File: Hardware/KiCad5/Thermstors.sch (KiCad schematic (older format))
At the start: 27 parts, among them J4 Audio-Jack-2_Switch, J5 Audio-Jack-2_Switch, U3 4066, U4 LM358

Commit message: Update schematic
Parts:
- removed J4, J5: Audio-Jack-2_Switch, symbol CloudSmoker-rescue:Audio-Jack-2_Switch
- removed U4: LM358, symbol CloudSmoker-rescue:LM358
- added C?: 10nF, symbol device:C
- added C?: 0.1u, symbol device:C
- added J? (x2): AudioJack2_SwitchT, symbol Connector:AudioJack2_SwitchT
- added U? (x5): 4066, symbol 4xxx:4066
- added U? (x3): LM358, symbol Amplifier_Operational:LM358
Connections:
- net +3V3: now also C?.1, C?.1, U?.14 (VDD), U?.8 (V+)
- net CTL-A: now also U?.13
- net CTL-B: now also U?.5
- net GND: now also C?.2, C?.2, J?.S, J?.S, U?.4 (V-), U?.7 (VSS)
- net MUX: now also U?.2, U?.3
- net MeatADC: now also U?.1
- net PitADC: now also U?.4
- net at R?.1, R?.2: now also J?.T (x2)
- net at R23.1, R25.2: now also U?.1
- net at R18.1, R23.2: now also U?.2 (-)
- net at R16.1, R20.2: now also U?.3 (+)
- net at R17.1, R21.2: now also U?.5 (+)
- net at R19.1, R24.2: now also U?.6 (-)
- net at R24.1, R26.2: now also U?.7
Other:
- note added: "OpAmp Level Shifter \n(approx 0.2 - 1.15V output for ESP8266 ADC)"
- note added: "Place cap as close to \nPin14 Vdd as possible"
- note added: "add 10nF cap as close to \nsupply pin as possible"
- note removed: "Level Shifter \n(approx 0.2 - 1.15V output for ESP8266 ADC)"
- note removed: "add 10nF cap between opamp V+ and gnd. as as possible"
- moved on the sheet: C7, C8, C9, R13, R14, R15, R16, R17, R18, R19, R20, R21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

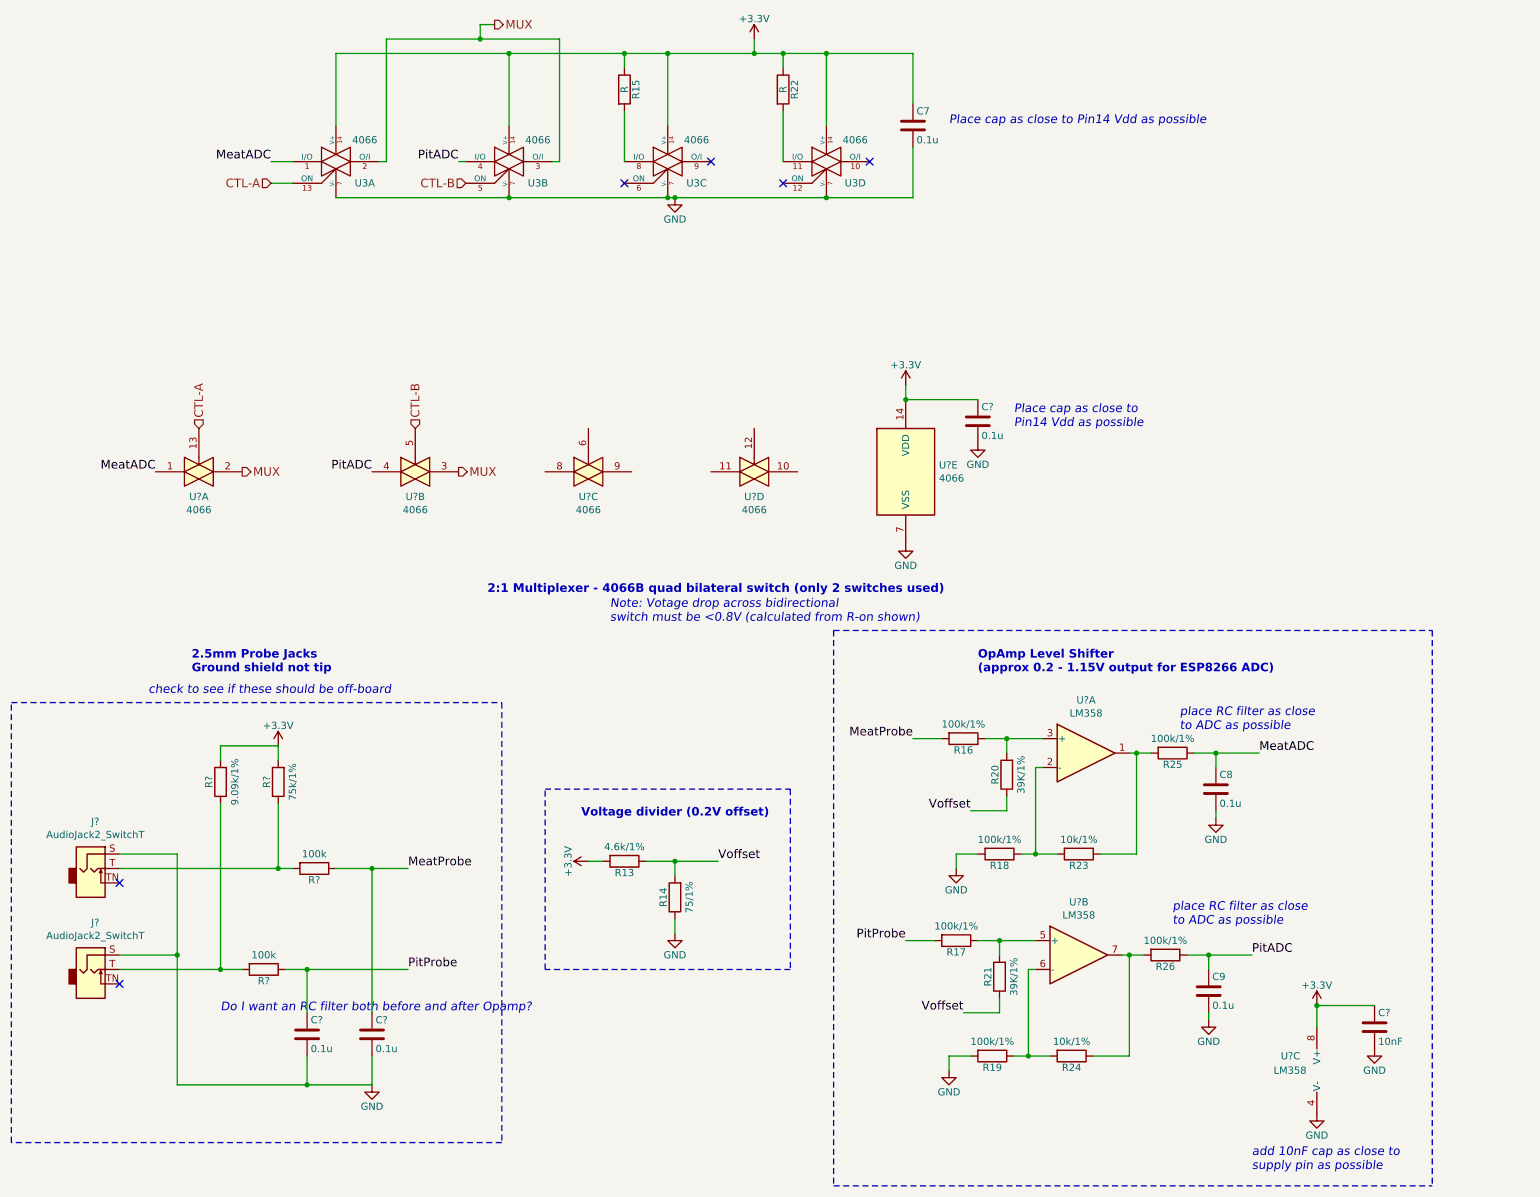
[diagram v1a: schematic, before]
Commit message: Schematic updates
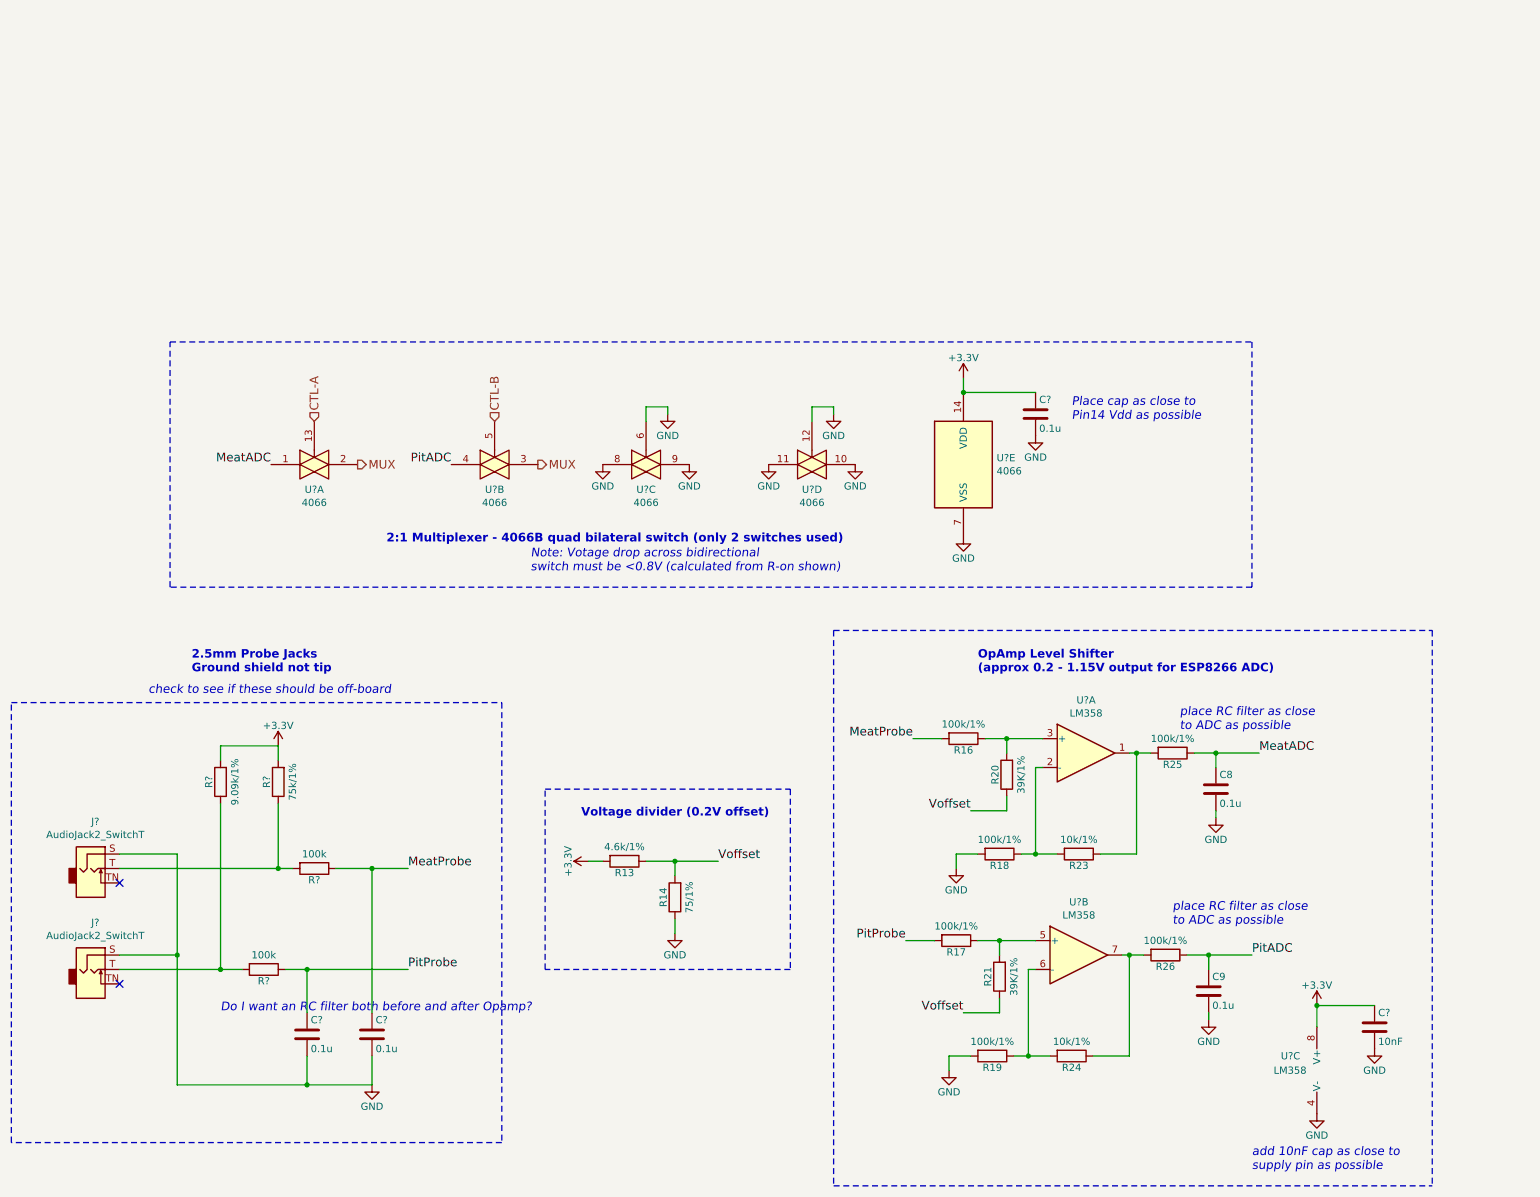
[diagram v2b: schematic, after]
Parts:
- removed C7: 0.1u, symbol device:C
- removed R15, R22: R, symbol device:R
- removed U3: 4066, symbol CloudSmoker-rescue:4066
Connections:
- net GND: now also U?.10, U?.11, U?.12, U?.6, U?.8, U?.9
- no-connect marks 6 -> 2
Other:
- note removed: "Place cap as close to Pin14 Vdd as possible"
- moved on the sheet: C?, U?A, U?B, U?C, U?D, U?E

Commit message: schematic updates
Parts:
- gave numbers to parts that had none: 12
- renumbered C9 to C10, C8 to C11, R13 to R17, R14 to R18, R17 to R19, R16 to R20, R19 to R21, R18 to R22, R21 to R23, R20 to R24, R24 to R25, R23 to R26, R26 to R27, R25 to R28
